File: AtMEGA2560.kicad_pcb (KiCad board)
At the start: 4 copper layers, 101.6 x 53.3 mm, 58 parts, among them J1 Conn_01x10, J10 Conn_02x02_Odd_Even, J11 Barrel_Jack_Switch, J2 Conn_02x18_Odd_Even, J3 Conn_01x08, J4 Conn_02x03_Odd_Even, J5 Conn_01x08, J6 Conn_02x03_Odd_Even, J7 Conn_01x08, J8 Conn_01x08, J9 USB_B, Q1 Q_PMOS_GSD, SW1 SW_Push, U1 ATmega2560-16AU, U2 NCP1117-5.0_SOT223, U3 ATmega16U2-AU, U4 LMV358, U5 LP2985-3.3, Y1 Resonator_Small, Y2 Crystal

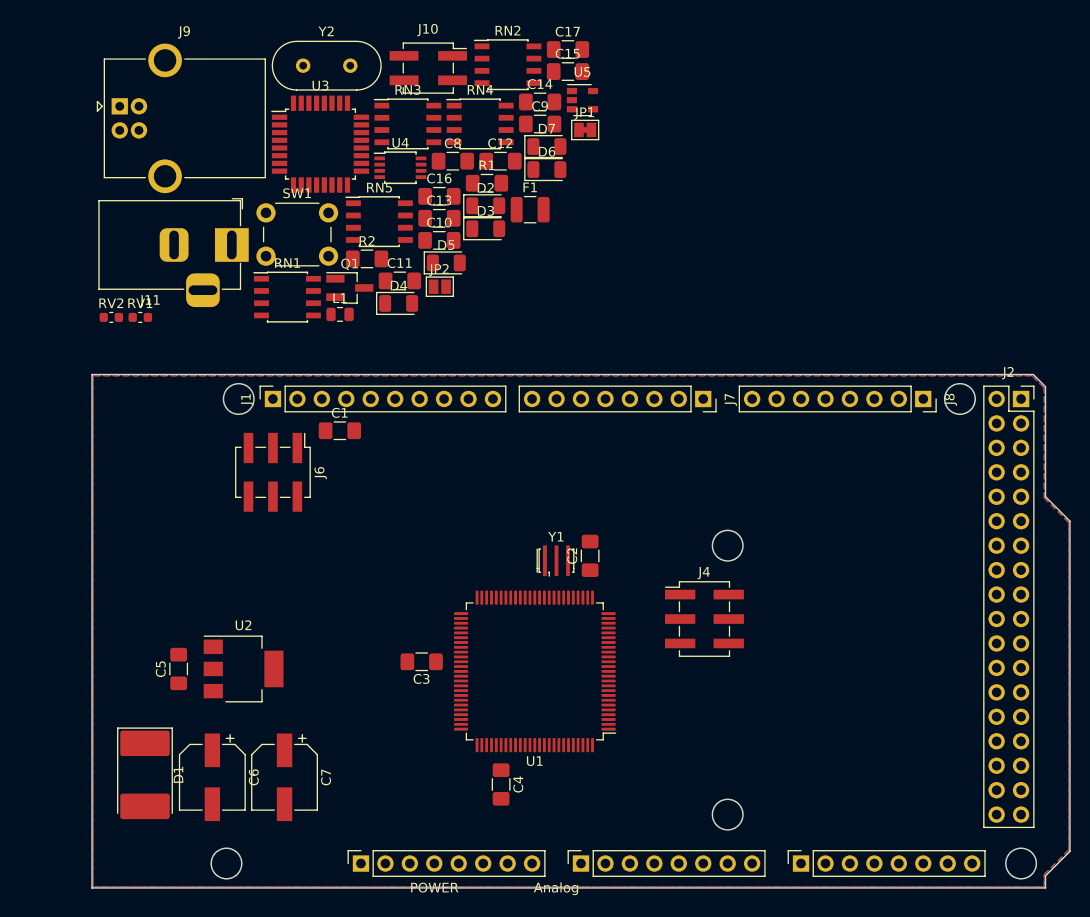
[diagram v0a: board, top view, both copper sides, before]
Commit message: Pin header instead of SMT
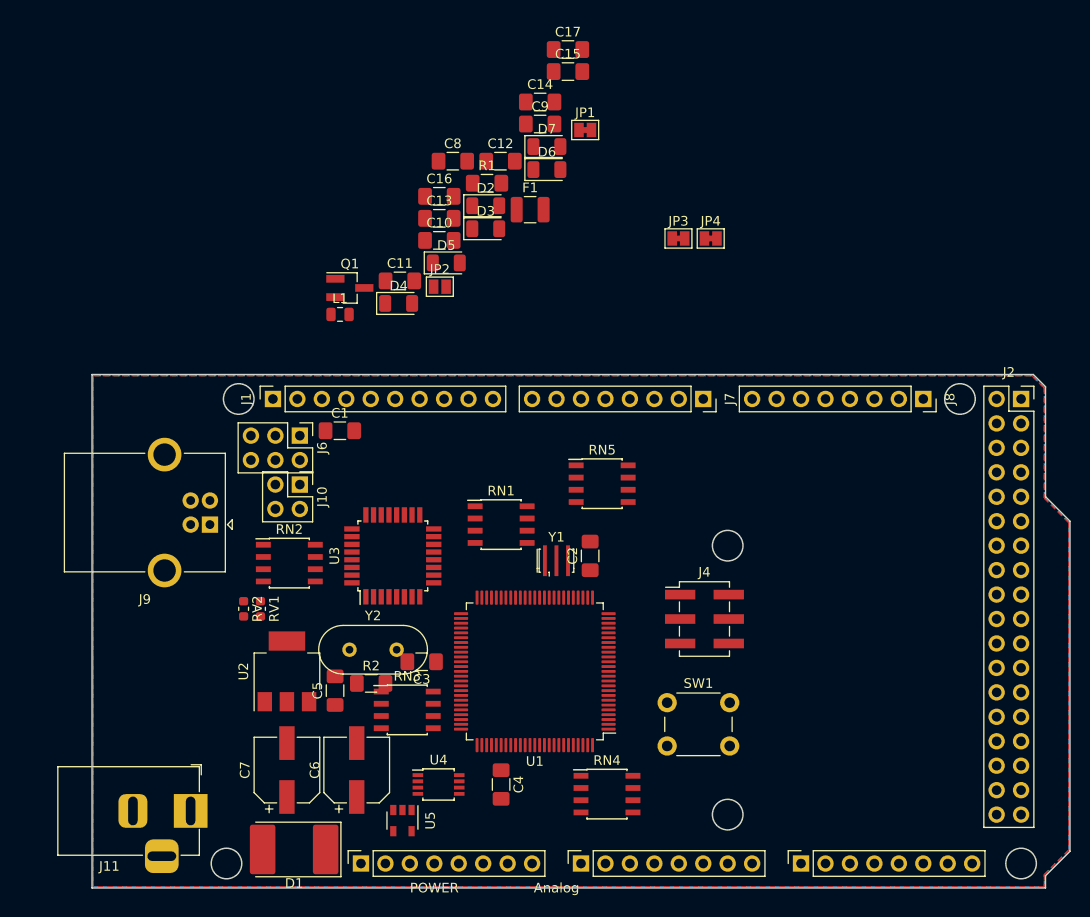
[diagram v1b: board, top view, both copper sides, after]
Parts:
- added JP3: SolderJumper_2_Bridged, Jumper:SolderJumper-2_P1.3mm_Bridged_Pad1.0x1.5mm, F.Cu at (137.1, 54.4)
- added JP4: SolderJumper_2_Bridged, Jumper:SolderJumper-2_P1.3mm_Bridged_Pad1.0x1.5mm, F.Cu at (140.5, 54.4)
- J10: footprint Connector_PinSocket_2.54mm:PinSocket_2x02_P2.54mm_Vertical_SMD -> Connector_PinHeader_2.54mm:PinHeader_2x02_P2.54mm_Vertical
- J6: footprint Connector_PinHeader_2.54mm:PinHeader_2x03_P2.54mm_Vertical_SMD -> Connector_PinHeader_2.54mm:PinHeader_2x03_P2.54mm_Vertical
- moved U5 77.1 mm to (108.5, 114.9), turned to 270 degrees
- moved RN4 70.9 mm to (129.7, 112.2)
- moved SW1 65.8 mm to (135.9, 102.7)
- moved U4 64.2 mm to (112.2, 111.2)
- moved RN3 60.9 mm to (109.0, 103.4)
- moved Y2 60.9 mm to (103.0, 97.2)
- moved J11 59.0 mm to (86.5, 113.9)
- moved RN2 56.5 mm to (96.7, 88.2)
- moved J10 45.3 mm to (97.8, 80.0), turned to 270 degrees
- moved J9 44.5 mm to (88.5, 84.2), turned to 180 degrees
- moved R2 44.1 mm to (105.2, 100.7)
- moved U3 43.4 mm to (107.5, 87.4), turned to 90 degrees
- moved RN5 35.7 mm to (129.2, 79.9)
- moved RV2 33.2 mm to (92.0, 92.9), turned to 270 degrees
- moved RV1 32.7 mm to (93.7, 92.9), turned to 270 degrees
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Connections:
- RN1 pad 2: SCL -> Net-(JP3-Pad2)
- RN1 pad 3: SDA -> Net-(JP4-Pad2)

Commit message: Labeling of components and location of connectors
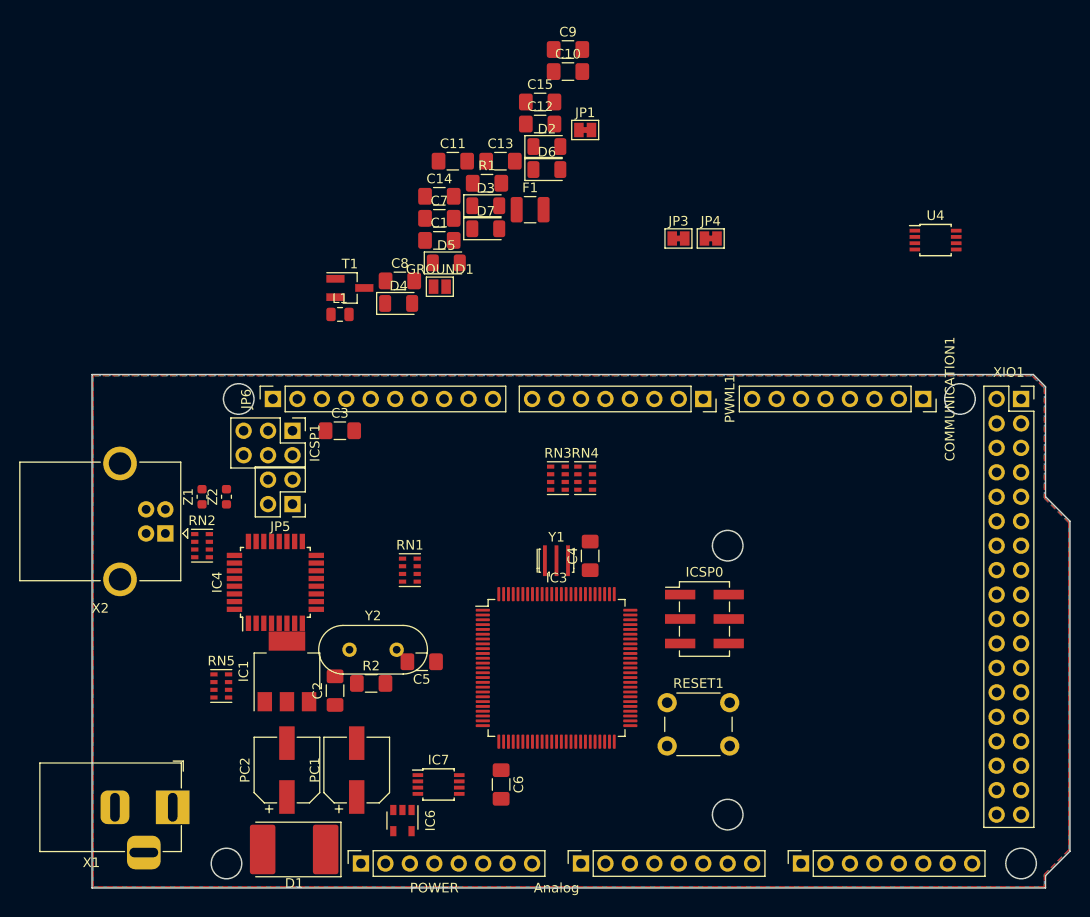
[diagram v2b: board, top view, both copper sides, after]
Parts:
- removed RV1, RV2: CG0603MLC-05E, Resistor_SMD:R_0603_1608Metric
- added U4: LMV358, Package_SO:TSSOP-8_3x3mm_P0.65mm, F.Cu at (163.8, 54.6)
- added Z1: CG0603MLC-05E, Resistor_SMD:R_0603_1608Metric, F.Cu at (87.6, 81.3)
- added Z2: CG0603MLC-05E, Resistor_SMD:R_0603_1608Metric, F.Cu at (90.2, 81.3)
- C2: renamed from C5; value C -> 100n
- C4: renamed from C2; value C -> 100n
- C5: renamed from C3; value C -> 100n
- C6: renamed from C4; value C -> 100n
- D1: value D -> M7
- D2: renamed from D7; value D -> CD1206-S01575
- D3: renamed from D2; value D -> CD1206-S01575
- D5: value YEL -> RX YELLOW
- D6: value YEL -> TX YELLOW
- F1: value Polyfuse -> MF-MSMF050-2 500mA
- IC7: renamed from U4; value LMV358 -> LMV358IDGKR
- JP1: value SolderJumper_2_Bridged -> RESET-EN
- PC2: renamed from C7; value CP -> 47u
- RN1, RN2, RN3, RN4, RN5: footprint Package_SO:SOIC-8_3.9x4.9mm_P1.27mm -> Resistor_SMD:R_Cat16-4
- T1: renamed from Q1; value Q_PMOS_GSD -> FDN340P
- X1: renamed from J11; value Barrel_Jack_Switch -> DC21MMX
- X2: renamed from J9; value USB_B -> USB-B_TH
- Y1: value Resonator_Small -> CSTCE16M0V53-R0 16MHZ
- Y2: value Crystal -> 16MHz
- moved RN5 44.8 mm to (89.6, 100.9)
- moved RN4 32.9 mm to (127.4, 79.3)
- moved RN3 28.7 mm to (124.6, 79.3)
- moved IC4 12.5 mm to (95.2, 90.2)
- moved RN1 10.6 mm to (109.2, 88.9)
- moved RN2 9.25 mm to (87.6, 86.4)
- moved X2 4.72 mm to (83.8, 85.1)
- moved IC3 2.29 mm to (124.5, 99.1), turned to 0 degrees
- moved JP5 2.17 mm to (97.0, 82.0), turned to 180 degrees
- moved X1 1.91 mm to (84.6, 113.5)
- moved ICSP1 0.92 mm to (97.0, 74.4)
- renumbered J3 to ADCH1, J5 to ADCL1, C10 to C1, C15 to C10, C8 to C11, C9 to C12, C12 to C13, C16 to C14, C14 to C15, C1 to C3, C13 to C7, C11 to C8, C17 to C9, J8 to COMMUNICATION1, D3 to D7, JP2 to GROUND1, U2 to IC1, U1 to IC3, U3 to IC4, U5 to IC6, J4 to ICSP0, J6 to ICSP1, J10 to JP5, J1 to JP6, C6 to PC1, J7 to PWML1, SW1 to RESET1, J2 to XIO1
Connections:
- net Net-(J6-Pad1) renamed /MISO2
- net Net-(J6-Pad3) renamed /SCK2
- net Net-(J6-Pad4) renamed /MOSI2
- C12 pad 1: Net-(C9-Pad1) -> Net-(C12-Pad1)
- IC4 pad 18: Net-(J10-Pad1) -> /PB4
- IC4 pad 19: Net-(J10-Pad3) -> /PB5
- IC4 pad 20: Net-(J10-Pad2) -> /PB6
- IC4 pad 21: Net-(J10-Pad4) -> PB7
- IC7 pad 1: Net-(RN3-Pad2) -> Net-(IC7-Pad1)
- IC7 pad 2: Net-(RN3-Pad2) -> +3V3
- IC7 pad 3: PB7 -> Net-(C12-Pad1)
- IC7 pad 4: GND -> (no net)
- IC7 pad 5: Net-(C9-Pad1) -> PB7
- IC7 pad 6: +3V3 -> Net-(IC7-Pad6)
- IC7 pad 7: Net-(Q1-Pad1) -> Net-(IC7-Pad6)
- IC7 pad 8: +5V -> (no net)
- JP5 pad 1: Net-(J10-Pad1) -> /PB4
- JP5 pad 2: Net-(J10-Pad2) -> /PB6
- JP5 pad 3: Net-(J10-Pad3) -> /PB5
- JP5 pad 4: Net-(J10-Pad4) -> PB7
- RN3 pad 2: Net-(RN3-Pad2) -> Net-(IC7-Pad6)
- RN5 pad 5: Net-(C9-Pad1) -> Net-(C12-Pad1)
- RN5 pad 6: Net-(C9-Pad1) -> Net-(C12-Pad1)
- T1 pad 1: Net-(Q1-Pad1) -> Net-(IC7-Pad1)

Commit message: IC4 net renaming PBx to 8PBx, PCB components movements to clear space for ethernet
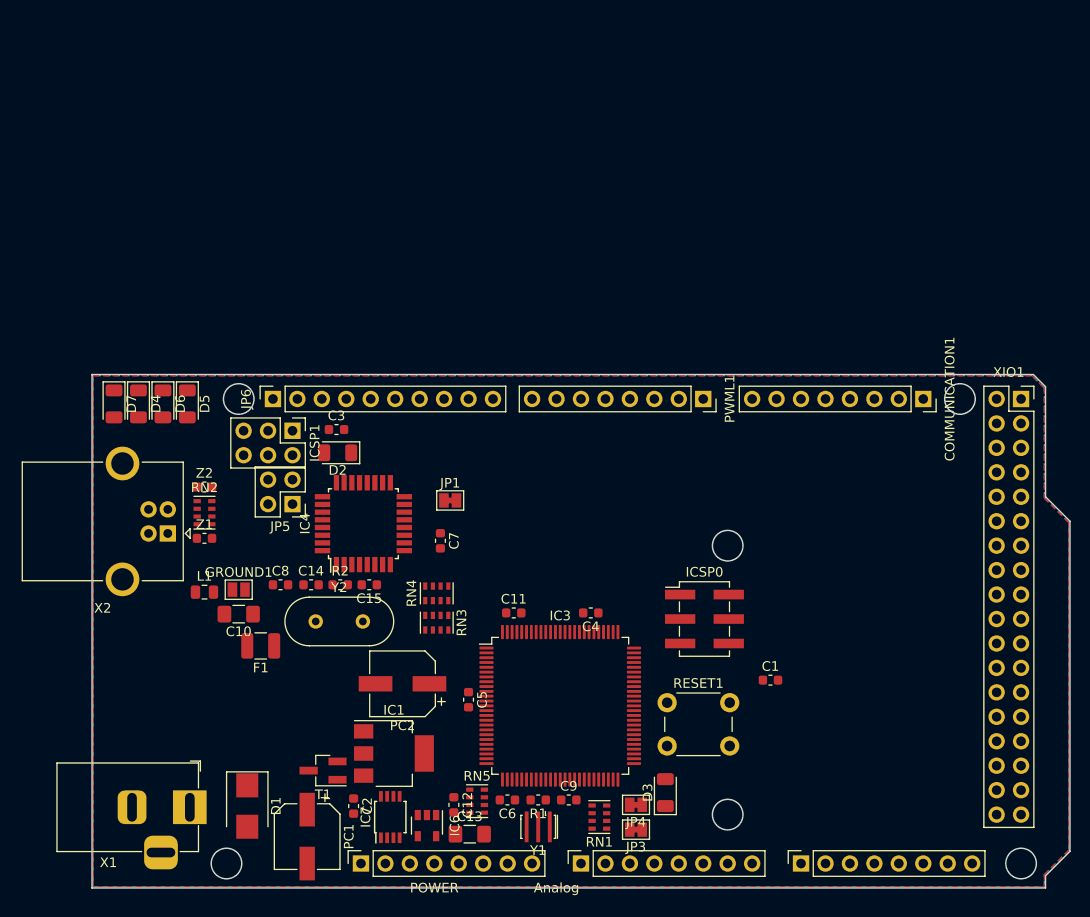
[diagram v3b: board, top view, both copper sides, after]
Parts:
- removed U4: LMV358, Package_SO:TSSOP-8_3x3mm_P0.65mm
- C1, C11, C12, C14, C15, C2, C3, C4, C5, C6, C7, C8, C9: footprint Capacitor_SMD:C_1206_3216Metric_Pad1.42x1.75mm_HandSolder -> Capacitor_SMD:C_0603_1608Metric
- D1: footprint Diode_SMD:D_3220_8050Metric_Pad2.65x5.15mm_HandSolder -> Diode_SMD:D_SMB
- R1, R2: footprint Resistor_SMD:R_1206_3216Metric_Pad1.42x1.75mm_HandSolder -> Resistor_SMD:R_0603_1608Metric
- moved C9 78.0 mm to (125.7, 112.8)
- moved C12 71.3 mm to (113.8, 113.3), turned to 270 degrees
- moved C13 70.0 mm to (115.4, 116.3)
- moved C10 65.9 mm to (91.4, 93.5), turned to 180 degrees
- moved R1 64.3 mm to (122.6, 112.8), turned to 180 degrees
- moved D3 63.8 mm to (135.8, 112.0), turned to 90 degrees
- moved JP3 61.6 mm to (132.7, 115.9), turned to 180 degrees
- moved JP4 59.3 mm to (132.7, 113.3), turned to 180 degrees
- moved C1 57.2 mm to (146.7, 100.3)
- moved F1 53.3 mm to (93.7, 96.8), turned to 180 degrees
- moved C15 53.2 mm to (105.0, 90.4), turned to 180 degrees
- moved T1 50.2 mm to (100.2, 109.7), turned to 180 degrees
- moved C11 47.4 mm to (120.0, 93.3)
- moved D6 46.7 mm to (83.6, 71.6), turned to 270 degrees
- moved D7 42.7 mm to (78.5, 71.6), turned to 270 degrees
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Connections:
- net Net-(IC3-Pad33) renamed /XTAL2
- net Net-(IC3-Pad34) renamed /XTAL1
- IC4 pad 18: /PB4 -> /8PB4
- IC4 pad 19: /PB5 -> /8PB5
- IC4 pad 20: /PB6 -> /8PB6
- IC4 pad 21: PB7 -> /8PB7
- IC7 pad 4: (no net) -> GND
- IC7 pad 8: (no net) -> +5V
- JP5 pad 1: /PB4 -> /8PB4
- JP5 pad 2: /PB6 -> /8PB6
- JP5 pad 3: /PB5 -> /8PB5
- JP5 pad 4: PB7 -> /8PB7

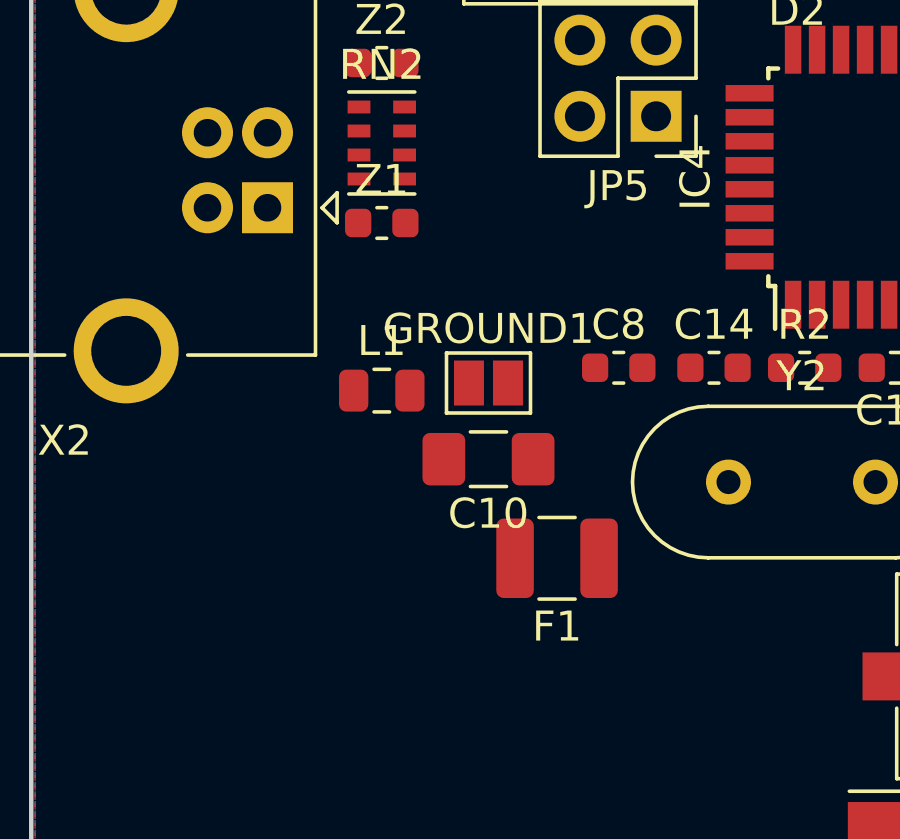
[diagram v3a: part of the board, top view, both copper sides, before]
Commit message: PCB components movements to clear space for ethernet
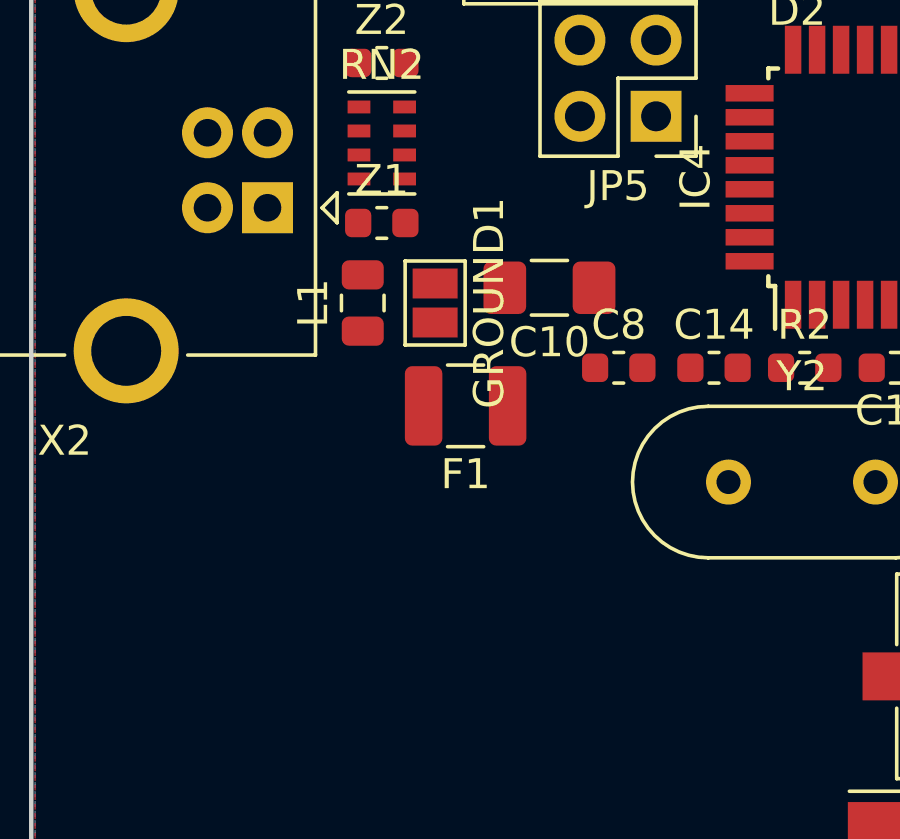
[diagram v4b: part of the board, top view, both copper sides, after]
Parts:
- moved C10 6.07 mm to (93.5, 87.8)
- moved F1 5.92 mm to (90.7, 91.7)
- moved GROUND1 3.21 mm to (89.7, 88.3), turned to 270 degrees
- moved L1 2.99 mm to (87.2, 88.3), turned to 90 degrees
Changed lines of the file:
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@@
   )
   (module Capacitor_SMD:C_1206_3216Metric_Pad1.42x1.75mm_HandSolder (layer F.Cu)
-    (at 91.44 93.472 180)
+    (at 93.472 87.757 180)
     (descr "Capacitor SMD 1206 (3216 Metric), square (rectangular) end terminal, IPC_7351 nominal with elongated pad for handsoldering. (Body size source: http://www.tortai-tech.com/upload/download/2011102023233369053.pdf), generated with kicad-footprint-generator")
     (tags "capacitor handsolder")
@@
   )
   (module Fuse:Fuse_1210_3225Metric (layer F.Cu)
-    (at 93.726 96.774 180)
+    (at 90.678 91.694 180)
     (descr "Fuse SMD 1210 (3225 Metric), square (rectangular) end terminal, IPC_7351 nominal, (Body size source: http://www.tortai-tech.com/upload/download/2011102023233369053.pdf), generated with kicad-footprint-generator")
     (tags resistor)
@@
   )
   (module Jumper:SolderJumper-2_P1.3mm_Open_Pad1.0x1.5mm (layer F.Cu)
-    (at 91.44 90.932)
+    (at 89.662 88.265 270)
     (descr "SMD Solder Jumper, 1x1.5mm Pads, 0.3mm gap, open")
     (tags "solder jumper open")
     (attr virtual)
-    (fp_text reference GROUND1 (at 0 -1.8) (layer F.SilkS)
-      (effects (font (size 1 1) (thickness 0.15)))
-    )
-    (fp_text value SolderJumper_2_Open (at 0 1.9) (layer F.Fab)
+    (fp_text reference GROUND1 (at 0 -1.8 270) (layer F.SilkS)
+      (effects (font (size 1 1) (thickness 0.15)))
+    )
+    (fp_text value SolderJumper_2_Open (at 0 1.9 270) (layer F.Fab)
       (effects (font (size 1 1) (thickness 0.15)))
     )
@@
     (fp_line (start 1.65 1.25) (end 1.65 -1.25) (layer F.CrtYd) (width 0.05))
     (fp_line (start 1.65 1.25) (end -1.65 1.25) (layer F.CrtYd) (width 0.05))
-    (pad 2 smd rect (at 0.65 0) (size 1 1.5) (layers F.Cu F.Mask)
+    (pad 2 smd rect (at 0.65 0 270) (size 1 1.5) (layers F.Cu F.Mask)
       (net 2 GND))
-    (pad 1 smd rect (at -0.65 0) (size 1 1.5) (layers F.Cu F.Mask)
+    (pad 1 smd rect (at -0.65 0 270) (size 1 1.5) (layers F.Cu F.Mask)
       (net 103 "Net-(C10-Pad2)"))
   )
   (module Inductor_SMD:L_0805_2012Metric (layer F.Cu)
-    (at 87.884 91.186)
+    (at 87.249 88.265 90)
     (descr "Inductor SMD 0805 (2012 Metric), square (rectangular) end terminal, IPC_7351 nominal, (Body size source: https://docs.google.com/spreadsheets/d/1BsfQQcO9C6DZCsRaXUlFlo91Tg2WpOkGARC1WS5S8t0/edit?usp=sharing), generated with kicad-footprint-generator")
     (tags inductor)
     (attr smd)
-    (fp_text reference L1 (at 0 -1.65) (layer F.SilkS)
-      (effects (font (size 1 1) (thickness 0.15)))
-    )
-    (fp_text value BLM21 (at 0 1.65) (layer F.Fab)
+    (fp_text reference L1 (at 0 -1.65 90) (layer F.SilkS)
+      (effects (font (size 1 1) (thickness 0.15)))
+    )
+    (fp_text value BLM21 (at 0 1.65 90) (layer F.Fab)
       (effects (font (size 1 1) (thickness 0.15)))
     )
@@
     (fp_line (start 1.68 -0.95) (end 1.68 0.95) (layer F.CrtYd) (width 0.05))
     (fp_line (start 1.68 0.95) (end -1.68 0.95) (layer F.CrtYd) (width 0.05))
-    (fp_text user %R (at 0 0) (layer F.Fab)
+    (fp_text user %R (at 0 0 90) (layer F.Fab)
       (effects (font (size 0.5 0.5) (thickness 0.08)))
     )
-    (pad 1 smd roundrect (at -0.9375 0) (size 0.975 1.4) (layers F.Cu F.Paste F.Mask) (roundrect_rratio 0.25)
+    (pad 1 smd roundrect (at -0.9375 0 90) (size 0.975 1.4) (layers F.Cu F.Paste F.Mask) (roundrect_rratio 0.25)
       (net 139 "Net-(L1-Pad1)"))
-    (pad 2 smd roundrect (at 0.9375 0) (size 0.975 1.4) (layers F.Cu F.Paste F.Mask) (roundrect_rratio 0.25)
+    (pad 2 smd roundrect (at 0.9375 0 90) (size 0.975 1.4) (layers F.Cu F.Paste F.Mask) (roundrect_rratio 0.25)
       (net 103 "Net-(C10-Pad2)"))
     (model ${KISYS3DMOD}/Inductor_SMD.3dshapes/L_0805_2012Metric.wrl
